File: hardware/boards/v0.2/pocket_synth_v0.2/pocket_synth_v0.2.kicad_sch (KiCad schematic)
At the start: 8 parts, among them SW1 SW_Push, SW2 SW_Push, SW3 SW_Push, SW4 SW_Push, U1 STM32H750XBHx, U2 STM32F401VEHx, U3 AS4C32M16SB-7BIN

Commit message: start rev2 schematic and layout
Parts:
- removed U1: STM32H750XBHx, Package_BGA:TFBGA-265_14x14mm_Layout17x17_P0.8mm, symbol MCU_ST_STM32H7:STM32H750XBHx
- added BT1: Battery, Connector_PinHeader_2.54mm:PinHeader_1x02_P2.54mm_Vertical, symbol Device:Battery
- added C1, C10, C11, C12, C13, C14, C15, C16, C17, C18, C19, C2, C20, C3, C6, C8, C9: 100nf, Capacitor_SMD:C_0402_1005Metric, symbol Device:C_Small
- added C21, C22, C5, C7: C, Capacitor_SMD:C_0805_2012Metric, symbol Device:C
- added C4: 4.7uF, Capacitor_SMD:C_0402_1005Metric, symbol Device:C_Small
- added J1: Conn_ARM_JTAG_SWD_10, Connector_PinHeader_1.27mm:PinHeader_2x05_P1.27mm_Vertical_SMD, symbol Connector:Conn_ARM_JTAG_SWD_10
- added J2: DEVICE, Connector_USB:USB_C_Receptacle_HCTL_HC-TYPE-C-16P-01A, symbol Connector:USB_C_Receptacle_USB2.0_16P
- added J3, J4, J5, J6: AudioJack3, Connector_Audio:Jack_3.5mm_CUI_SJ-3523-SMT_Horizontal, symbol Connector_Audio:AudioJack3
- added J7: DISPLAY, Connector_FFC-FPC:Amphenol_F32Q-1A7x1-11053_1x53-1MP_P0.5mm_Horizontal, symbol Connector:Conn_01x54_Socket
- added J8: Micro_SD_Card_Det2, Connector_Card:microSD_HC_Hirose_DM3AT-SF-PEJM5, symbol Connector:Micro_SD_Card_Det2
- added J9: HOST, Connector_USB:USB_C_Receptacle_HCTL_HC-TYPE-C-16P-01A, symbol Connector:USB_C_Receptacle_USB2.0_16P
- added U1: STM32H743XIHx, Package_BGA:TFBGA-265_14x14mm_Layout17x17_P0.8mm, symbol MCU_ST_STM32H7:STM32H743XIHx
- added U4: STM32H753VIHx, Package_BGA:TFBGA-100_8x8mm_Layout10x10_P0.8mm, symbol MCU_ST_STM32H7:STM32H753VIHx
- added U5: W25Q128JVS, Package_SO:SOIC-8_5.3x5.3mm_P1.27mm, symbol Memory_Flash:W25Q128JVS
- added U6: SDRAM1, Package_BGA:Alliance_TFBGA-54_8x8mm_Layout9x9_P0.8mm, symbol AS4C32M16SB-7BIN:AS4C32M16SB-7BIN
- added Y1: 32.768kHz, Crystal:Crystal_SMD_Abracon_ABM10-4Pin_2.5x2.0mm, symbol Device:Crystal_GND23
- added Y2: HSE, Crystal:Crystal_SMD_Abracon_ABM10-4Pin_2.5x2.0mm, symbol Device:Crystal_GND23
- U3: value AS4C32M16SB-7BIN -> SDRAM0; footprint Package_BGA:FBGA-96_8x13mm_Layout9x16_P0.8mm -> Package_BGA:Alliance_TFBGA-54_8x8mm_Layout9x9_P0.8mm
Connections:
- net VDDQ is gone; now on net +3.3V: U3.A7 (VDDQ), U3.B3 (VDDQ), U3.C7 (VDDQ), U3.D3 (VDDQ)
- net VSSQ is gone; now on net GND: U3.A3 (VSSQ), U3.B7 (VSSQ), U3.C3 (VSSQ), U3.D7 (VSSQ)
- net FMC_D15: now reaches U3.A2 (DQ15)
- net FMC_D15: now also U1.T16 (PD10), U6.A2 (DQ15)
- net FMC_D0: now reaches U3.A8 (DQ0)
- net FMC_D0: now also U1.P16 (PD14), U6.A8 (DQ0)
- net FMC_D14: now reaches U3.B1 (DQ14)
- net FMC_D14: now also U1.T17 (PD9), U6.B1 (DQ14)
- net FMC_D13: now reaches U3.B2 (DQ13)
- net FMC_D13: now also U1.U16 (PD8), U6.B2 (DQ13)
- net FMC_D2: now reaches U3.B8 (DQ2)
- net FMC_D2: now also U1.D13 (PD0), U6.B8 (DQ2)
- net FMC_D1: now reaches U3.B9 (DQ1)
- net FMC_D1: now also U1.P15 (PD15), U6.B9 (DQ1)
- net FMC_D12: now reaches U3.C1 (DQ12)
- net FMC_D12: now also U1.R11 (PE15), U6.C1 (DQ12)
- net FMC_D11: now reaches U3.C2 (DQ11)
- net FMC_D11: now also U1.U10 (PE14), U6.C2 (DQ11)
- net FMC_D4: now reaches U3.C8 (DQ4)
- net FMC_D4: now also U1.U9 (PE7), U6.C8 (DQ4)
- net FMC_D3: now reaches U3.C9 (DQ3)
- net FMC_D3: now also U1.E12 (PD1), U6.C9 (DQ3)
- net FMC_D10: now reaches U3.D1 (DQ10)
- net FMC_D10: now also U1.T10 (PE13), U6.D1 (DQ10)
- net FMC_D9: now reaches U3.D2 (DQ9)
- net FMC_D9: now also U1.R10 (PE12), U6.D2 (DQ9)
- net FMC_D6: now reaches U3.D8 (DQ6)
- net FMC_D6: now also U1.P9 (PE9), U6.D8 (DQ6)
- net FMC_D5: now reaches U3.D9 (DQ5)
- net FMC_D5: now also U1.T9 (PE8), U6.D9 (DQ5)
- net FMC_D8: now reaches U3.E1 (DQ8)
- net FMC_D8: now also U1.P10 (PE11), U6.E1 (DQ8)
- net FMC_NBL0: now reaches U3.E8 (LDQM)
- net FMC_NBL0: now also U1.C4 (PE0), U6.E8 (LDQM)
- net FMC_D7: now reaches U3.E9 (DQ7)
- net FMC_D7: now also U1.N9 (PE10), U6.E9 (DQ7)
- net FMC_NBL1: now reaches U3.F1 (UDQM)
- net FMC_NBL1: now also U1.B4 (PE1), U6.F1 (UDQM)
- net FMC_CLK: now reaches U3.F2 (CLK)
- net FMC_CLK: now also U1.B12 (PD3), U6.F2 (CLK)
- net FMC_SDCKE0: now reaches U3.F3 (CKE)
- net FMC_SDCKE0: now also U1.U4 (PC5)
- net FMC_SDNCAS: now reaches U3.F7 (~{CAS})
- net FMC_SDNCAS: now also U1.D6 (PG15), U6.F7 (~{CAS})
- net FMC_SDNRAS: now reaches U3.F8 (~{RAS})
- net FMC_SDNRAS: now also U1.T7 (PF11), U6.F8 (~{RAS})
- net FMC_SDNWE: now reaches U3.F9 (~{WE})
- net FMC_SDNWE: now also U1.P4 (PH5), U6.F9 (~{WE})
- net FMC_A12: now reaches U3.G1 (A12)
- net FMC_A12: now also U1.H16 (PG2), U6.G1 (A12)
- net FMC_A11: now reaches U3.G2 (A11)
- net FMC_A11: now also U1.U8 (PG1), U6.G2 (A11)
- net FMC_A8: now reaches U3.G3 (A9)
- net FMC_A8: now also U3.H1 (A8), U1.P8 (PF14), U1.R9 (PF15), U6.G3 (A9), U6.H1 (A8)
- net FMC_BA0: now reaches U3.G7 (BA0)
- net FMC_BA0: now also U1.H14 (PG4), U6.G7 (BA0)
- net FMC_BA1: now reaches U3.G8 (BA1)
- net FMC_BA1: now also U1.G14 (PG5), U6.G8 (BA1)
- net FMC_SDNE0: now reaches U3.G9 (~{CS})
- net FMC_SDNE0: now also U1.P2 (PH3)
- net FMC_A7: now reaches U3.H2 (A7)
- net FMC_A7: now also U1.P7 (PF13), U6.H2 (A7)
- net FMC_A6: now reaches U3.H3 (A6)
- net FMC_A6: now also U1.R7 (PF12), U6.H3 (A6)
- net FMC_A0: now reaches U3.H7 (A0)
- net FMC_A0: now also U1.G4 (PF0), U6.H7 (A0)
- net FMC_A1: now reaches U3.H8 (A1)
- net FMC_A1: now also U1.G3 (PF1), U6.H8 (A1)
- net FMC_A10: now reaches U3.H9 (A10)
- net FMC_A10: now also U1.T8 (PG0), U6.H9 (A10)
- net FMC_A5: now reaches U3.J2 (A5)
- net FMC_A5: now also U1.J4 (PF5), U6.J2 (A5)
- net FMC_A4: now reaches U3.J3 (A4)
- net FMC_A4: now also U1.J5 (PF4), U6.J3 (A4)
- net FMC_A3: now reaches U3.J7 (A3)
- net FMC_A3: now also U1.H4 (PF3), U6.J7 (A3)
- net FMC_A2: now reaches U3.J8 (A2)
- net FMC_A2: now also U1.G1 (PF2), U6.J8 (A2)
- net VDD renamed +3.3V
- net +3.3V: now also C1.1, C10.1, C11.1, C12.1, C13.1, C14.1, C15.1, C16.1, C17.1, C18.1, C19.1, C2.1, C20.1, C3.1, C4.1, C6.1, C8.1, C9.1, J1.1 (VTref), J8.4 (VDD), U1.E11 (VDD), U1.E6 (VDD), U1.E9 (VDD), U1.F5 (VDD), U1.G13 (VDD), U1.G5 (VDD), U1.H13 (VDD), U1.H5 (VDD), U1.J13 (VDD), U1.K13 (VDD), U1.K5 (VDD), U1.L13 (VDD), U1.L5 (VDD), U1.M13 (VDD), U1.M5 (VDD), U1.N10 (VDD), U1.N11 (VDD), U1.N12 (VDD), U1.N7 (VDD), U1.N8 (VDD), U1.P17 (VDD), U6.A7 (VDDQ), U6.A9 (VDD), U6.B3 (VDDQ), U6.C7 (VDDQ), U6.D3 (VDDQ), U6.E7 (VDD), U6.J9 (VDD)
- net VSS renamed GND
- net GND: now also C1.2, C10.2, C11.2, C12.2, C13.2, C14.2, C15.2, C16.2, C17.2, C18.2, C19.2, C2.2, C20.2, C21.2, C22.2, C3.2, C4.2, C5.2, C6.2, C7.2, C8.2, C9.2, J1.3 (GND), J1.5 (GND), J1.9 (GNDDetect), J2.A1 (GND), J2.A12 (GND), J2.B1 (GND), J2.B12 (GND), J2.S1 (SHIELD), J7.53 (Pin_53), J7.54 (Pin_54), J8.11 (SHIELD), J9.A1 (GND), J9.A12 (GND), J9.B1 (GND), J9.B12 (GND), J9.S1 (SHIELD), U1.A1 (VSS), U1.A17 (VSS), U1.B2 (VSS), U1.B6 (VSS), U1.C10 (VSS), U1.C13 (VSS), U1.C16 (VSS), U1.F1 (VSS), U1.F2 (VSS), U1.G10 (VSS), U1.G11 (VSS), U1.G16 (VSS), U1.G2 (VSS), U1.G7 (VSS), U1.G8 (VSS), U1.G9 (VSS), U1.H10 (VSS), U1.H11 (VSS), U1.H7 (VSS), U1.H8 (VSS), U1.H9 (VSS), U1.J10 (VSS), U1.J11 (VSS), U1.J16 (VSS), U1.J17 (VSS), U1.J3 (VSS), U1.J7 (VSS), U1.J8 (VSS), U1.J9 (VSS), U1.K10 (VSS), U1.K11 (VSS), U1.K15 (VSS), U1.K7 (VSS), U1.K8 (VSS), U1.K9 (VSS), U1.L10 (VSS), U1.L11 (VSS), U1.L15 (VSS), U1.L7 (VSS), U1.L8 (VSS), U1.L9 (VSS), U1.M15 (VSS), U1.N16 (VSS), U1.P1 (VSSA), U1.R4 (VSS), U1.R8 (VSS), U1.T12 (VSS), U1.U1 (VSS), U1.U17 (VSS), U5.4 (GND), U6.A1 (VSS), U6.A3 (VSSQ), U6.B7 (VSSQ), U6.C3 (VSSQ), U6.D7 (VSSQ), U6.E3 (VSS), U6.J1 (VSS), Y1.3, Y2.3
- new net: C7.1, U1.C2 (PC14), Y1.4
- new net: C22.1, U1.J1 (PH1), Y2.1
- new net: C21.1, U1.J2 (PH0), Y2.4
- new net: J9.A4 (VBUS), J9.A9 (VBUS), J9.B4 (VBUS), J9.B9 (VBUS)
- new net: C5.1, U1.C1 (PC15), Y1.1
- new net: U4.C2 (VSS), U4.E4 (VSS), U4.E5 (VSS), U4.E6 (VSS), U4.J1 (VSS)
- new net +BATT: BT1.1 (+)
- new net -BATT: BT1.2 (-)
- new net FMC_NE1: U1.C11 (PD7), U6.G9 (~{CS})
- new net FMC_SDCKE1: U1.U13 (PH7), U6.F3 (CKE)
- new net LCD_B0: J7.12 (Pin_12), U1.D11 (PJ12)
- new net LCD_B1: J7.13 (Pin_13), U1.E10 (PJ13)
- new net LCD_B2: J7.14 (Pin_14), U1.D10 (PJ14)
- new net LCD_B3: J7.15 (Pin_15), U1.B10 (PJ15)
- new net LCD_B4: J7.16 (Pin_16), U1.C8 (PK3)
- new net LCD_B5: J7.17 (Pin_17), U1.B8 (PK4)
- new net LCD_B6: J7.18 (Pin_18), U1.A8 (PK5)
- new net LCD_B7: J7.19 (Pin_19), U1.C7 (PK6)
- new net LCD_CLK: J7.38 (Pin_38), U1.H3 (PI14)
- new net LCD_DE: U1.D7 (PK7)
- new net LCD_G0: J7.20 (Pin_20), U1.N14 (PJ7)
- new net LCD_G1: J7.21 (Pin_21), U1.N13 (PJ8)
- new net LCD_G2: J7.22 (Pin_22), U1.M14 (PJ9)
- new net LCD_G3: J7.23 (Pin_23), U1.L14 (PJ10)
- new net LCD_G4: J7.24 (Pin_24), U1.K14 (PJ11)
- new net LCD_G5: J7.25 (Pin_25), U1.J14 (PK0)
- new net LCD_G6: J7.26 (Pin_26), U1.J15 (PK1)
- new net LCD_G7: J7.27 (Pin_27), U1.H17 (PK2)
- new net LCD_HSYNC: J7.36 (Pin_36)
- new net LCD_LEDA: J7.3 (Pin_3), J7.4 (Pin_4)
- new net LCD_LEDK: J7.1 (Pin_1), J7.2 (Pin_2)
- new net LCD_R0: J7.28 (Pin_28), U1.P5 (PI15)
- new net LCD_R1: J7.29 (Pin_29), U1.N6 (PJ0)
- new net LCD_R2: J7.30 (Pin_30), U1.P6 (PJ1)
- new net LCD_R3: J7.31 (Pin_31), U1.T6 (PJ2)
- new net LCD_R4: J7.32 (Pin_32), U1.U6 (PJ3)
- new net LCD_R5: J7.33 (Pin_33), U1.U7 (PJ4)
- new net LCD_R6: J7.34 (Pin_34), U1.R12 (PJ5)
- new net LCD_R7: J7.35 (Pin_35), U1.N15 (PJ6)
- new net LCD_RESET: J7.8 (Pin_8)
- new net LCD_SPI_CLK: J7.10 (Pin_10)
- new net LCD_SPI_CS: J7.9 (Pin_9)
- new net LCD_SPI_PICO: J7.11 (Pin_11)
- new net LCD_VSYNC: J7.37 (Pin_37)
- new net QSPI1_CLK: U1.L3 (PF10), U5.6 (CLK)
- new net QSPI1_CS: U1.G15 (PG6), U5.1 (~{CS})
- new net QSPI1_IO0: U1.K4 (PF8), U5.5 (DI/IO_{0})
- new net QSPI1_IO1: U1.L4 (PF9), U5.2 (DO/IO_{1})
- new net QSPI1_IO2: U1.K3 (PF7), U5.3 (~{WP}/IO_{2})
- new net QSPI1_IO3: U1.K2 (PF6), U5.7 (~{HOLD}/~{RESET}/IO_{3})
- new net SDMMC1_CK: J8.5 (CLK), U1.C12 (PC12)
- new net SDMMC1_CMD: J8.3 (CMD), U1.D12 (PD2)
- new net SDMMC1_D0: J8.7 (DAT0), U1.E13 (PC8)
- new net SDMMC1_D1: J8.8 (DAT1), U1.E14 (PC9)
- new net SDMMC1_D2: J8.1 (DAT2), U1.A13 (PC10)
- new net SDMMC1_D3: J8.2 (DAT3/CD), U1.B13 (PC11)
- new net SWD_CLK: J1.4 (SWCLK/TCK), U1.B14 (PA14)
- new net SWD_IO: J1.2 (SWDIO/TMS), U1.C15 (PA13)
- new net SWD_RESET: J1.10 (~{RESET}), U1.K1 (NRST)
- new net SWD_SWO: J1.6 (SWO/TDO), U1.C6 (PB3)
- new net USB_FS_D+: J9.A6 (D+), J9.B6 (D+), U1.E16 (PA12)
- new net USB_FS_D-: J9.A7 (D-), J9.B7 (D-), U1.E17 (PA11)
- new net USB_HS_D+: J2.A6 (D+), J2.B6 (D+), U1.T15 (PB15)
- new net USB_HS_D-: J2.A7 (D-), J2.B7 (D-), U1.U15 (PB14)
- new net VBUS: J2.A4 (VBUS), J2.A9 (VBUS), J2.B4 (VBUS), J2.B9 (VBUS)
- no-connect marks 0 -> 17
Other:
- note added: "Audio Board"
- note added: "Input Board"
- note added: "STM32s with LCD support: STM32F429 - UFBGA169, UFBGA176, LQFP176, WLCSP143, LQFP208, TFBGA216 STM32F429NI - $10-16 STM32F429BI - $8-16 STM32F469 - UFBGA169, UFBGA176, LQFP176, WLCSP143, LQFP208, TFBGA216 STM32F469NI - $16-20 STM32F469BI - $16-24"
- note added: "https://www.buydisplay.com/3-5-inch-ips-tft-display-optl-capacitive-touch-lq035nc111-lq035nc211 https://www.buydisplay.com/ips-3-5-inch-full-viewing-640x480-tft-display-capacitive-touch-screen"
- moved on the sheet: MK2, SW1, SW2, SW3, SW4, U2, U3

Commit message: start SDRAM routing
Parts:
- removed U2: STM32F401VEHx, Package_BGA:UFBGA-100_7x7mm_Layout12x12_P0.5mm, symbol MCU_ST_STM32F4:STM32F401VEHx
- added H1, H2: MountingHole_Pad, MountingHole:MountingHole_2.2mm_M2_Pad, symbol Mechanical:MountingHole_Pad
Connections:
- net FMC_A8: no longer U1.R9 (PF15), U3.G3 (A9), U6.G3 (A9)
- new net FMC_A9: U1.R9 (PF15), U3.G3 (A9), U6.G3 (A9)
- no-connect marks 17 -> 18

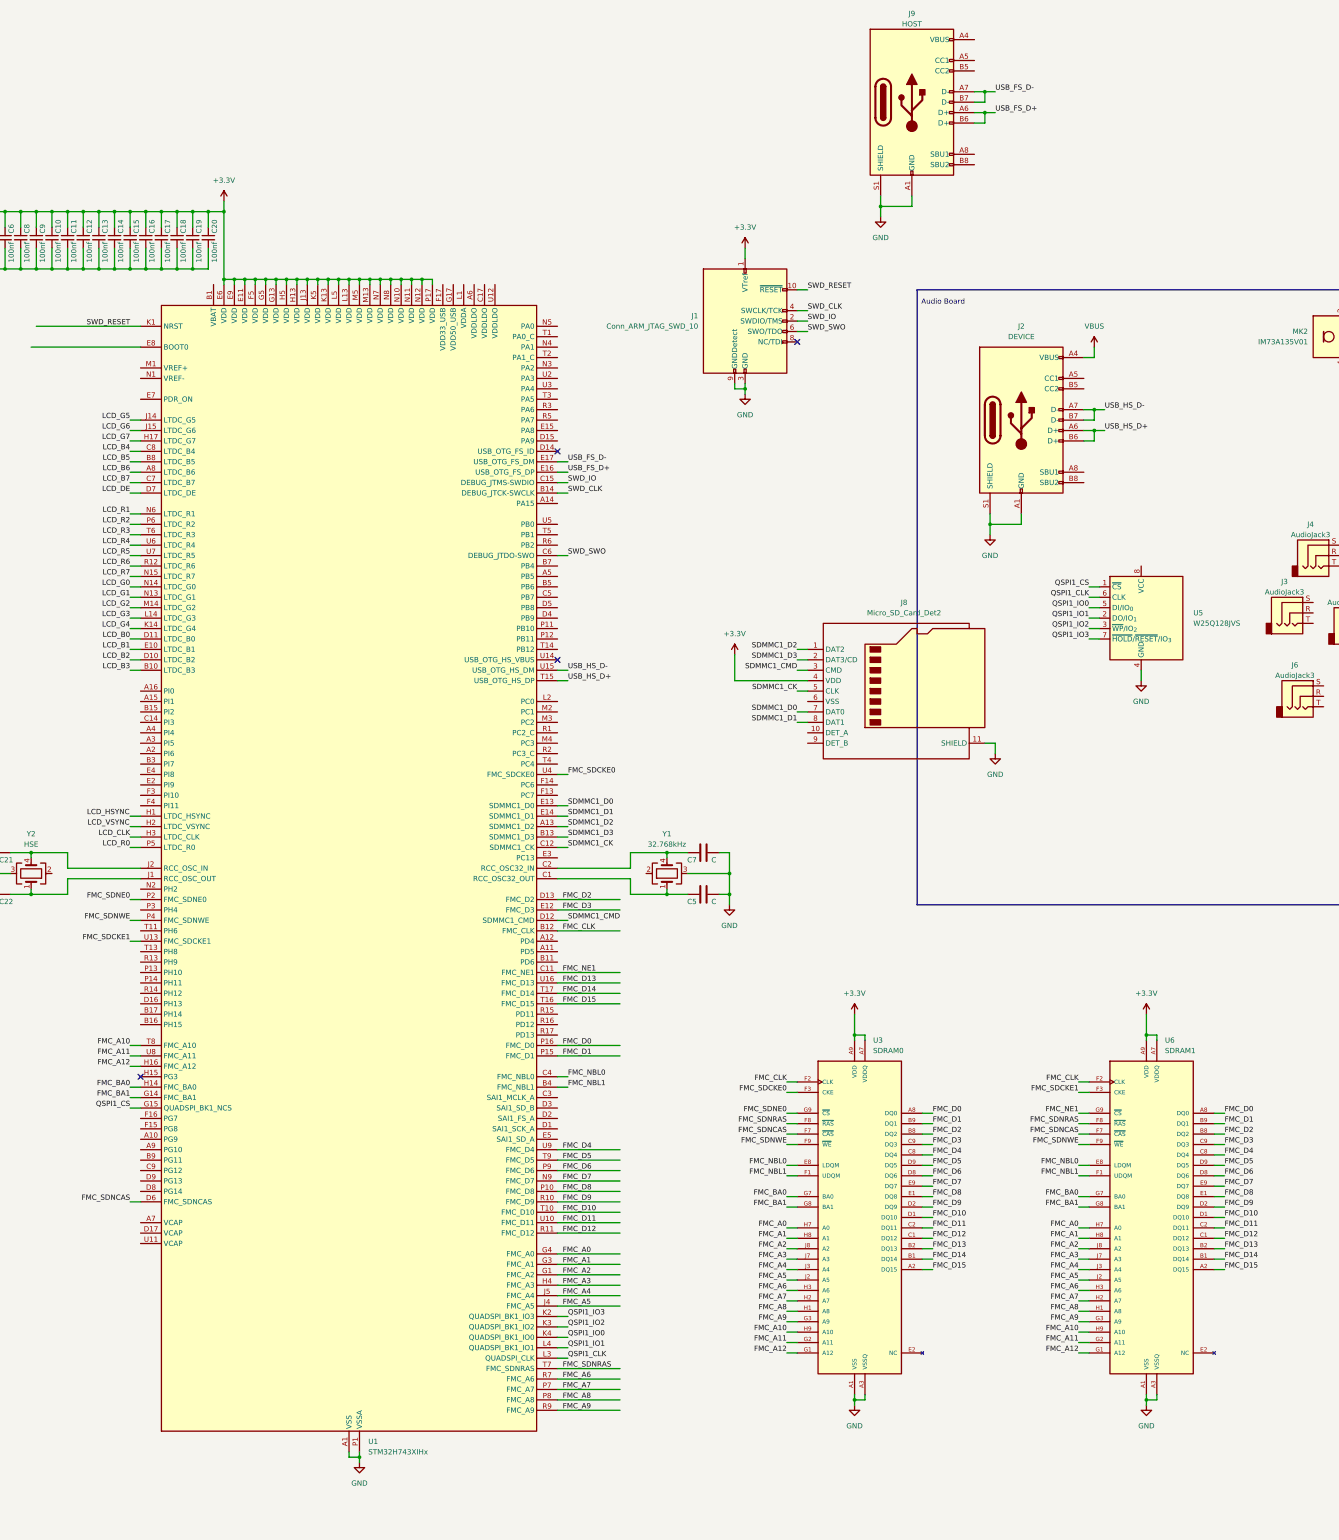
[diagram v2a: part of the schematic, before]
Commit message: routed right side of SDRAM
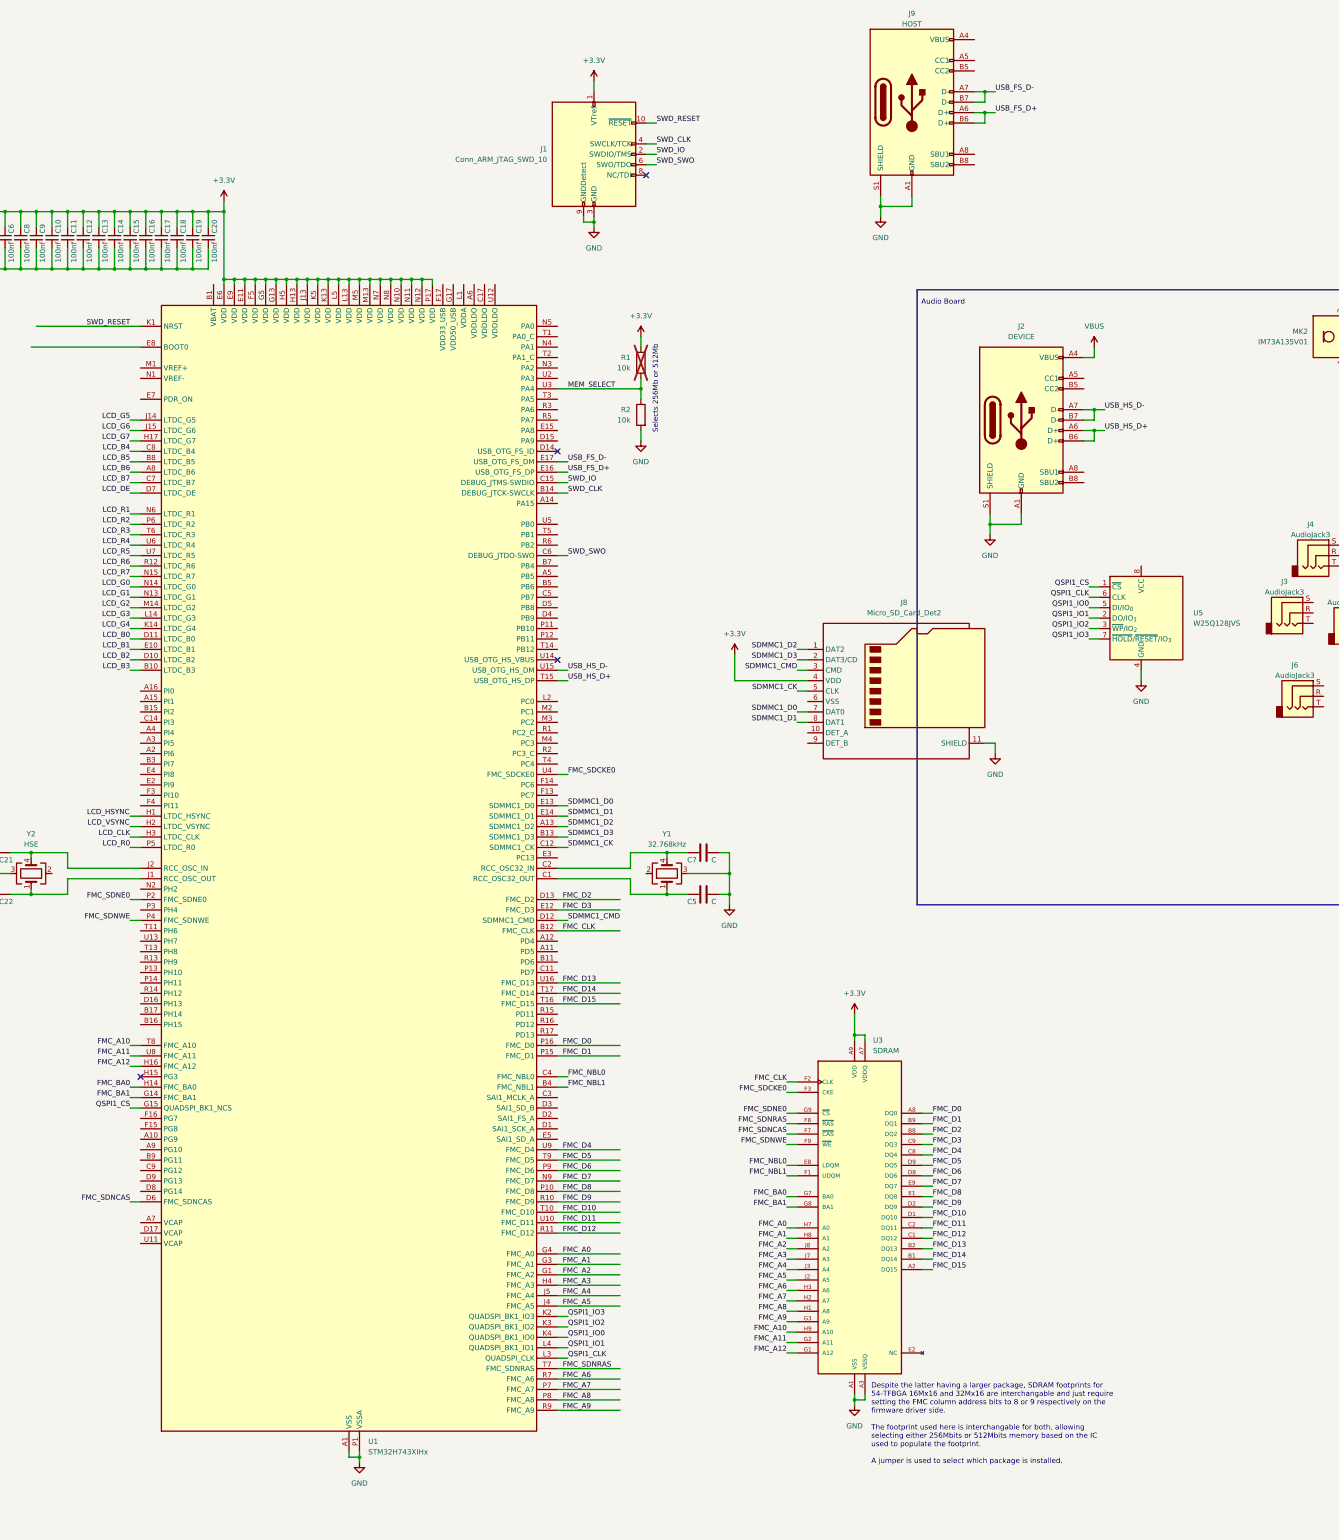
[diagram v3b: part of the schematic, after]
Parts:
- removed U6: SDRAM1, Package_BGA:Alliance_TFBGA-54_8x8mm_Layout9x9_P0.8mm, symbol AS4C32M16SB-7BIN:AS4C32M16SB-7BIN
- added R1, R2: 10k, Resistor_SMD:R_0603_1608Metric_Pad0.98x0.95mm_HandSolder, symbol Device:R
- U3: value SDRAM0 -> SDRAM; footprint Package_BGA:Alliance_TFBGA-54_8x8mm_Layout9x9_P0.8mm -> S42S16320F-7BLI:IC54_IS42S16320F-7BLI_ISI
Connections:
- net +3.3V: now also R1.1
- net GND: now also R2.2
- net MEM_SELECT: now reaches U1.U3 (PA4)
- net MEM_SELECT: now also R1.2, R2.1
- net FMC_NE1: no longer names the net of U1.C11 (PD7)
- net FMC_SDCKE1: no longer names the net of U1.U13 (PH7)
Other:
- note added: "Despite the latter having a larger package, SDRAM footprints for 54-TFBGA 16Mx16 and 32Mx16 are interchangable and just require setting the FMC column address bits to 8 or 9 respectively on the firmware driver side. The footprint used here is interchangable for both, allowing selecting either 256Mbits or 512Mbits memory based on the IC used to populate the footprint. A jumper is used to select wh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"
- note added: "Selects 256Mb or 512Mb"
- moved on the sheet: J1

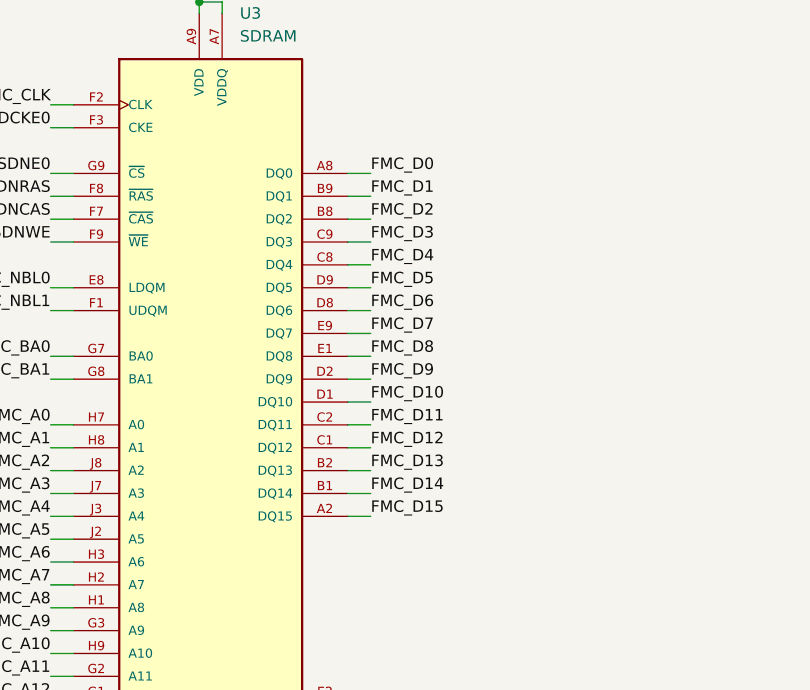
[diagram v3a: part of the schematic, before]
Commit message: more SDRAM routing
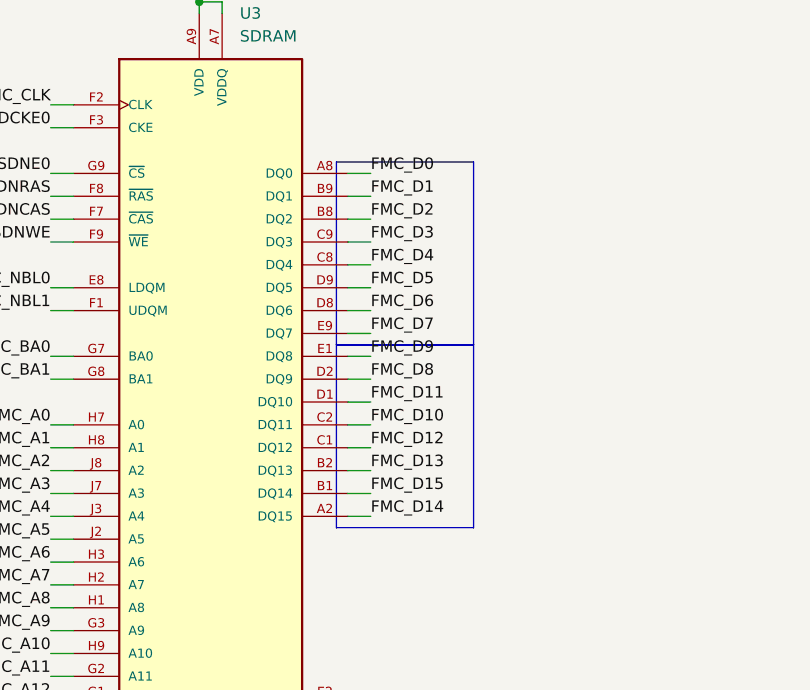
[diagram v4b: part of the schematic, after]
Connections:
- net FMC_D10: now also U3.C2 (DQ11); no longer U3.D1 (DQ10)
- net FMC_D11: now also U3.D1 (DQ10); no longer U3.C2 (DQ11)
- net FMC_D14: now also U3.A2 (DQ15); no longer U3.B1 (DQ14)
- net FMC_D15: now also U3.B1 (DQ14); no longer U3.A2 (DQ15)
- net FMC_D8: now also U3.D2 (DQ9); no longer U3.E1 (DQ8)
- net FMC_D9: now also U3.E1 (DQ8); no longer U3.D2 (DQ9)
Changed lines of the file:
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@@
 	)
 	(rectangle
+		(start 269.24 257.81)
+		(end 284.48 278.13)
+		(stroke
+			(width 0)
+			(type default)
+		)
+		(fill
+			(type none)
+		)
+	)
+	(rectangle
 		(start 269.24 58.42)
 		(end 439.42 208.28)
@@
 		)
 	)
+	(rectangle
+		(start 269.24 278.13)
+		(end 284.48 298.45)
+		(stroke
+			(width 0)
+			(type default)
+		)
+		(fill
+			(type none)
+		)
+	)
 	(text "Audio Board"
 		(exclude_from_sim no)
@@
 	)
 	(label "FMC_D15"
-		(at 273.05 297.18 0)
+		(at 273.05 294.64 0)
 		(effects
 			(font
@@
 	)
 	(label "FMC_D11"
-		(at 273.05 287.02 0)
+		(at 273.05 284.48 0)
 		(effects
 			(font
@@
 	)
 	(label "FMC_D8"
-		(at 273.05 279.4 0)
+		(at 273.05 281.94 0)
 		(effects
 			(font
@@
 	)
 	(label "FMC_D9"
-		(at 273.05 281.94 0)
+		(at 273.05 279.4 0)
 		(effects
 			(font
@@
 	)
 	(label "FMC_D10"
-		(at 273.05 284.48 0)
+		(at 273.05 287.02 0)
 		(effects
 			(font
@@
 	)
 	(label "FMC_D14"
-		(at 273.05 294.64 0)
+		(at 273.05 297.18 0)
 		(effects
 			(font

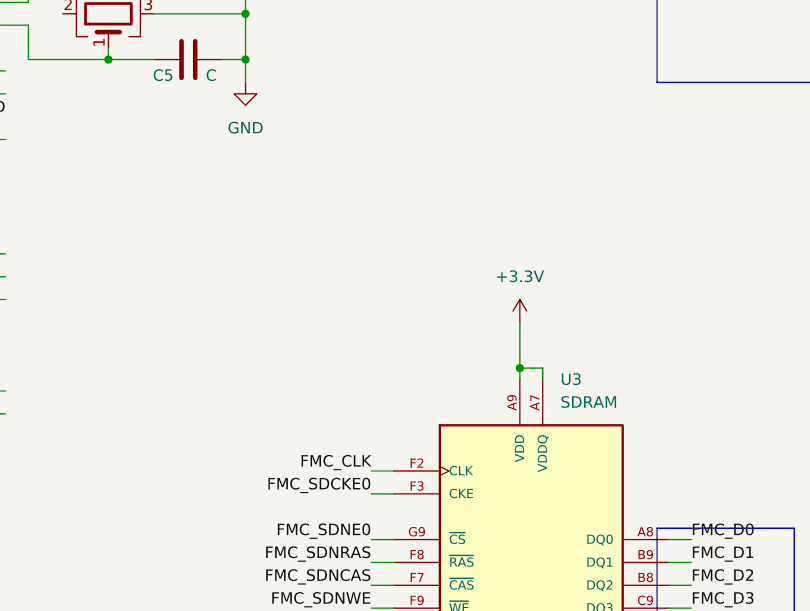
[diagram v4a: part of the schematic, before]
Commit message: finish routing SDRAM
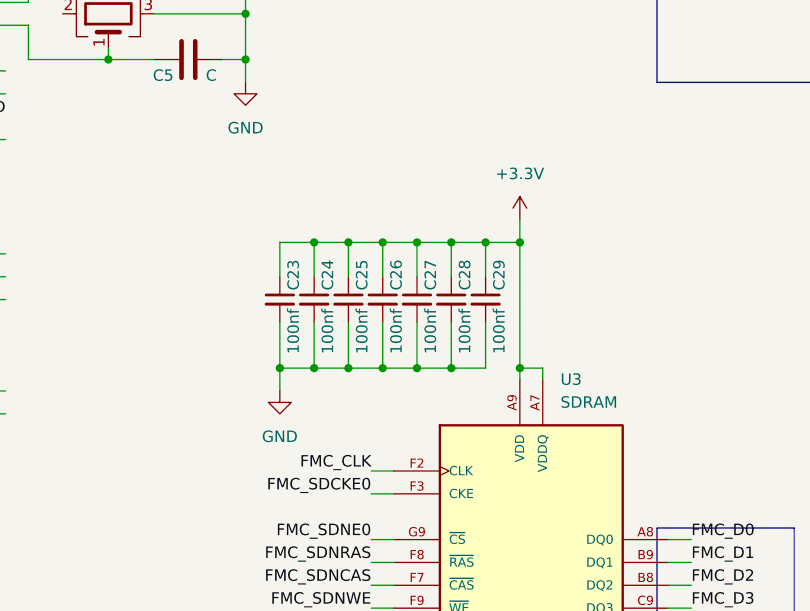
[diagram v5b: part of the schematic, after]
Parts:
- added C23, C24, C25, C26, C27, C28, C29: 100nf, Capacitor_SMD:C_0402_1005Metric, symbol Device:C_Small
- BT1: footprint Connector_PinHeader_2.54mm:PinHeader_1x02_P2.54mm_Vertical -> Connector_JST:JST_PH_S2B-PH-K_1x02_P2.00mm_Horizontal
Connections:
- net +3.3V: now also C23.1, C24.1, C25.1, C26.1, C27.1, C28.1, C29.1
- net GND: now also C23.2, C24.2, C25.2, C26.2, C27.2, C28.2, C29.2

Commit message: routed display FPC
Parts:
- J7: footprint Connector_FFC-FPC:Amphenol_F32Q-1A7x1-11053_1x53-1MP_P0.5mm_Horizontal -> Connector_FFC-FPC:Amphenol_F32Q-1A7x1-11054_1x54-1MP_P0.5mm_Horizontal
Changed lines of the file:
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@@
 			)
 		)
-		(property "Footprint" "Connector_FFC-FPC:Amphenol_F32Q-1A7x1-11053_1x53-1MP_P0.5mm_Horizontal"
+		(property "Footprint" "Connector_FFC-FPC:Amphenol_F32Q-1A7x1-11054_1x54-1MP_P0.5mm_Horizontal"
 			(at -12.7 151.13 0)
 			(effects
@@
 			)
 		)
-		(property "Datasheet" "~"
+		(property "Datasheet" "https://www.buydisplay.com/3-5-inch-ips-tft-display-optl-capacitive-touch-lq035nc111-lq035nc211"
 			(at -12.7 151.13 0)
 			(effects
